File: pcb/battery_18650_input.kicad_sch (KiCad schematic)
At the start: 21 parts, among them Q1 AO3400A, Q2 8205A, U5 MAX17320

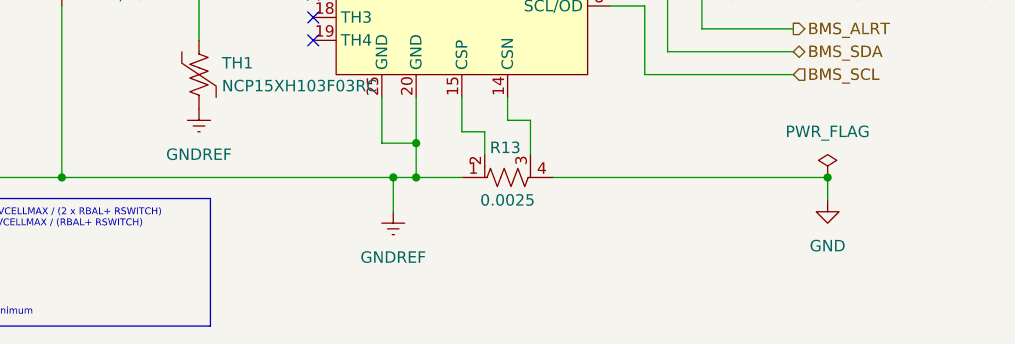
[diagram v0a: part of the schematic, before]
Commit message: Add U4 decoupling cap, source U15 MPN, improve GND/GNDREF visual distinction
- Add local decoupling capacitor to U4 (74LVC1G08) VCC/GND
- Add missing Manf/MPN/LCSC Part# to U15 (PCA9555PWR, TI, C2864778) found
  during a full net-trace design review
- Color all GNDREF net wires in battery_18650_input.kicad_sch orange to
  make the intentional GND/GNDREF current-sense split (bridged only by
  R13) visually obvious on the canvas, not just from the net name
- Add a schematic text note at R13 documenting the split for reviewers
  without access to CLAUDE.md

Co-Authored-By: Claude Sonnet 5 <noreply@anthropic.com>
Claude-Session: https://claude.ai/code/session_01LhLkuH6sQ5GbUZ61bG7p2h
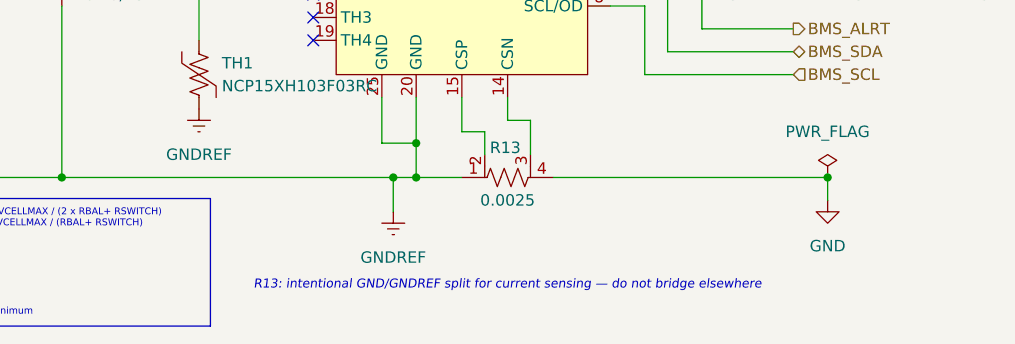
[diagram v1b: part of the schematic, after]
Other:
- note added: "R13: intentional GND/GNDREF split for current sensing — do not bridge elsewhere"
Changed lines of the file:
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@@
 			(width 0)
 			(type default)
+			(color 255 140 0 1)
 		)
 	)
@@
 			(width 0)
 			(type default)
+			(color 255 140 0 1)
 		)
 	)
@@
 			(width 0)
 			(type default)
+			(color 255 140 0 1)
 		)
 	)
@@
 			(width 0)
 			(type default)
+			(color 255 140 0 1)
 		)
 	)
@@
 			(width 0)
 			(type default)
+			(color 255 140 0 1)
 		)
 	)
@@
 			(width 0)
 			(type default)
+			(color 255 140 0 1)
 		)
 	)
@@
 			(width 0)
 			(type default)
+			(color 255 140 0 1)
 		)
 	)
@@
 			(width 0)
 			(type default)
+			(color 255 140 0 1)
 		)
 	)
@@
 			(width 0)
 			(type default)
+			(color 255 140 0 1)
 		)
 	)
@@
 			(width 0)
 			(type default)
+			(color 255 140 0 1)
 		)
 	)
@@
 			(width 0)
 			(type default)
+			(color 255 140 0 1)
 		)
 	)
@@
 			(width 0)
 			(type default)
+			(color 255 140 0 1)
 		)
 	)
@@
 			(width 0)
 			(type default)
+			(color 255 140 0 1)
 		)
 	)
@@
 			(width 0)
 			(type default)
+			(color 255 140 0 1)
 		)
 	)
@@
 			(width 0)
 			(type default)
+			(color 255 140 0 1)
 		)
 	)
@@
 			(width 0)
 			(type default)
+			(color 255 140 0 1)
 		)
 	)
@@
 			(width 0)
 			(type default)
+			(color 255 140 0 1)
 		)
 	)
@@
 			(width 0)
 			(type default)
+			(color 255 140 0 1)
 		)
 	)
@@
 		)
 	)
+  (text "R13: intentional GND/GNDREF split for current sensing — do not bridge elsewhere"
+    (at 152.4 139.7 0)
+    (effects (font (size 1 1) (italic yes) (color 255 140 0 1)) (justify top))
+  )
 	(symbol
 		(lib_id "power:GNDREF")
